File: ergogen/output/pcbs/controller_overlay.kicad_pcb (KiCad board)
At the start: 2 copper layers, 19.7 x 60.1 mm, 2 parts

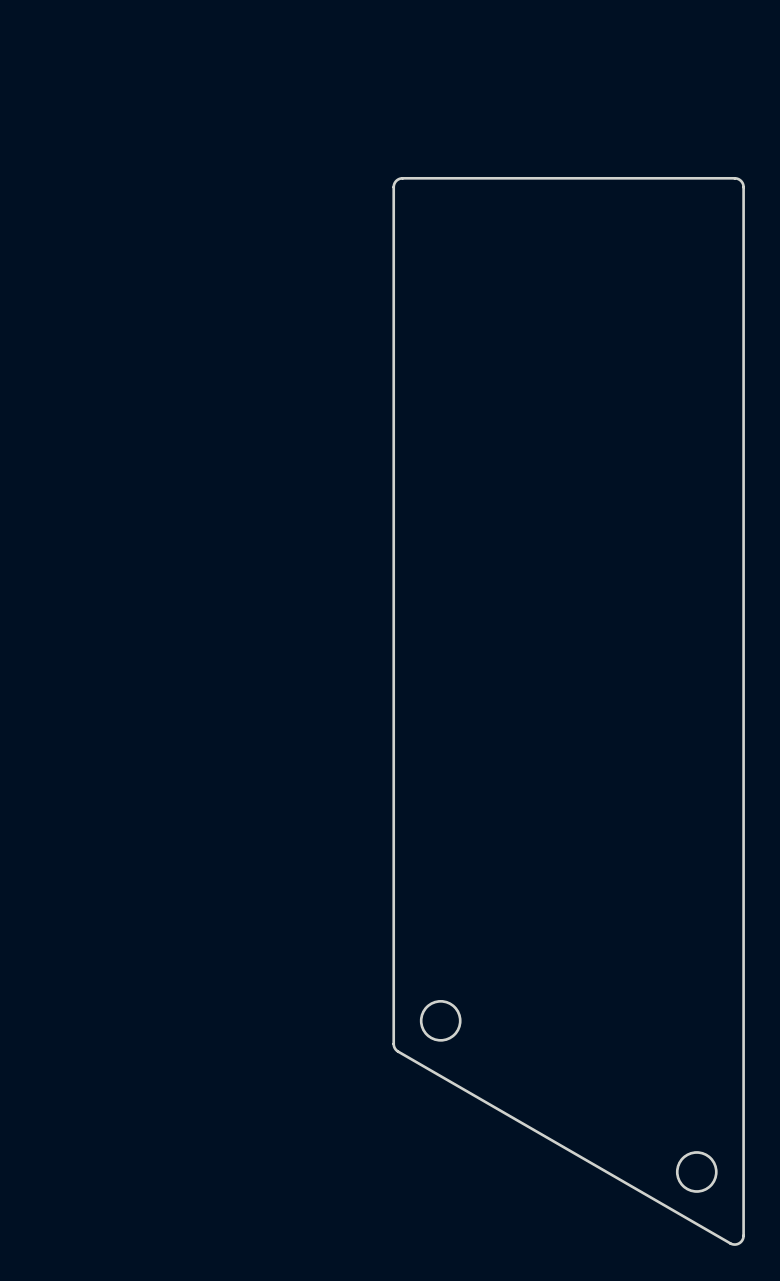
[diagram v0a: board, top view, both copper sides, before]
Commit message: Removed outer column
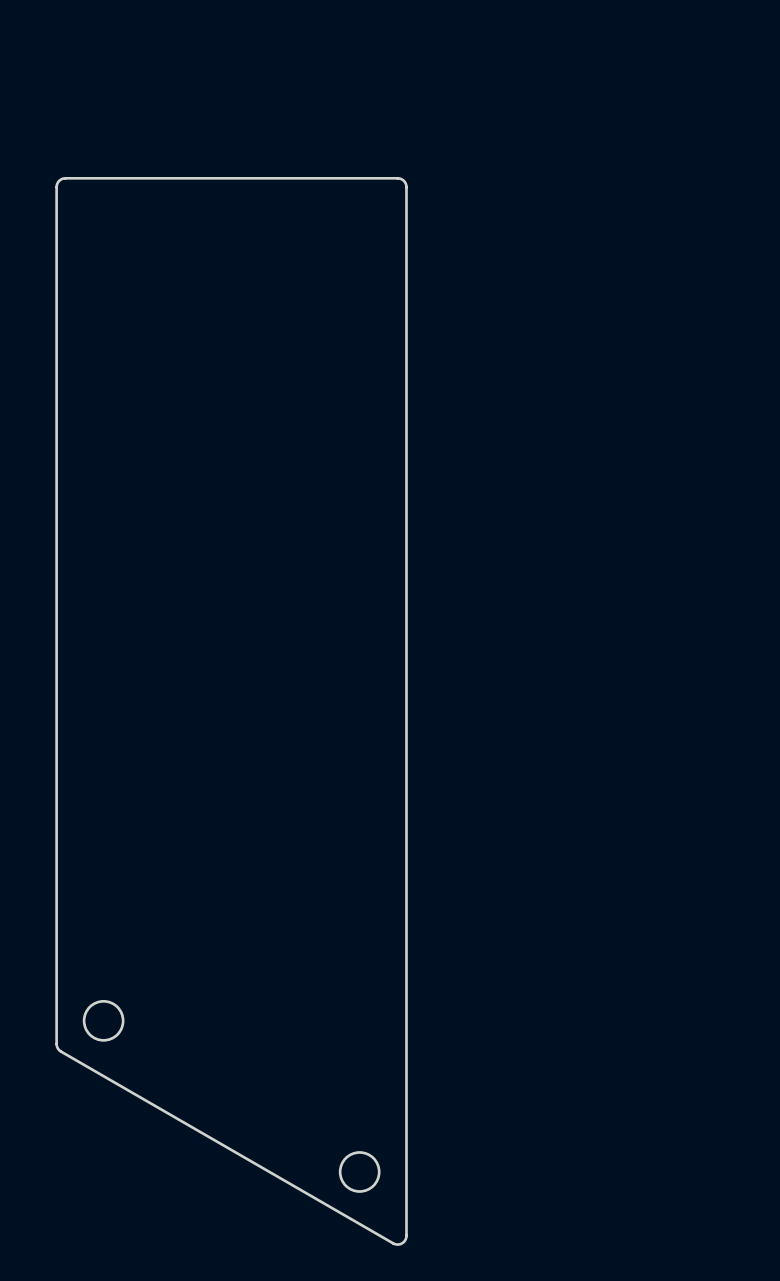
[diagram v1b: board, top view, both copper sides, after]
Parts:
- moved MH1 19.0 mm to (188.8, 100.5)
- moved MH2 19.0 mm to (203.2, 109.0)

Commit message: Changed stagger to be like karia
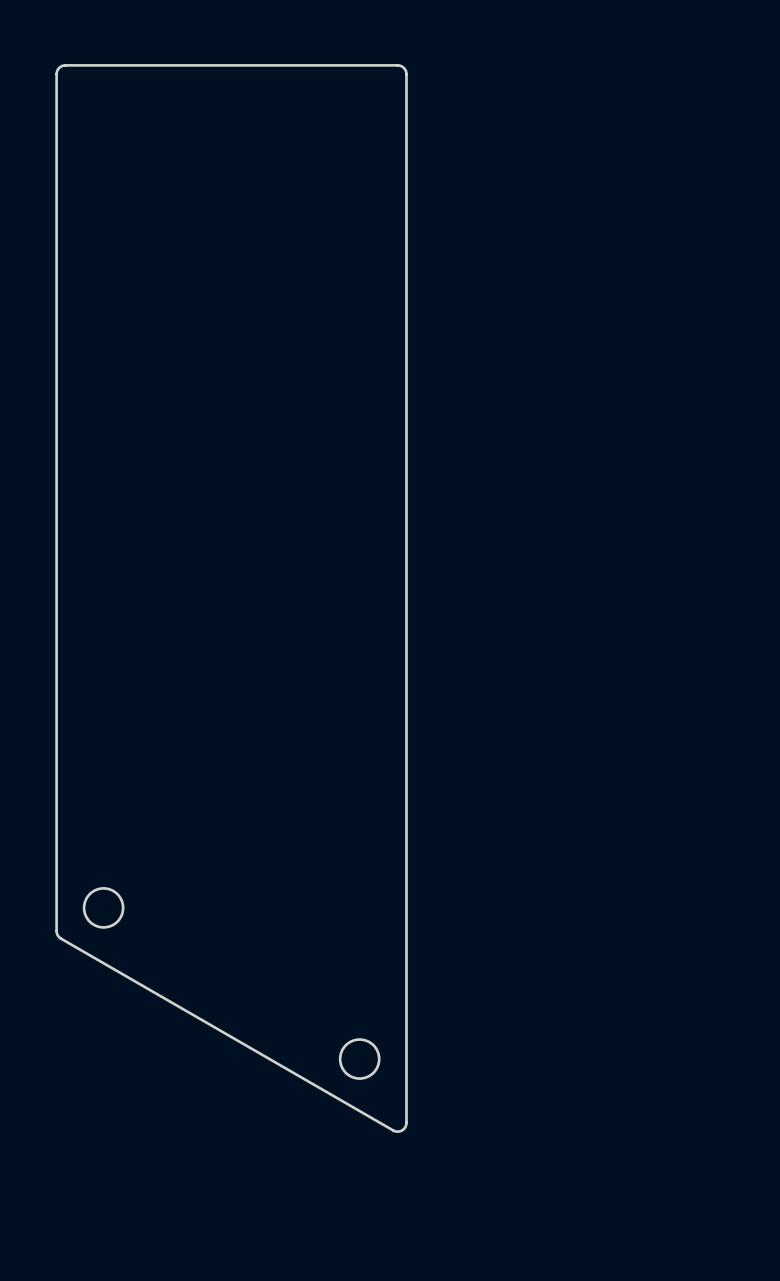
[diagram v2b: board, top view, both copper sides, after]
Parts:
- moved MH1 6.36 mm to (188.8, 94.1)
- moved MH2 6.36 mm to (203.2, 102.6)
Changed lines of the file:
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@@
   (net 0 "")
   (module "ceoloide:mounting_hole_npth" (layer F.Cu)
-      (at 188.762 100.476 0)
+      (at 188.762 94.111 0)
       (fp_text reference "MH1" (at 0 2.55 0) (layer F.SilkS) hide (effects (font (size 1 1) (thickness 0.15))))
       (pad "" np_thru_hole circle (at 0 0 0) (size 2.2 2.2) (drill 2.2) (layers *.Cu *.Mask))
   )
   (module "ceoloide:mounting_hole_npth" (layer F.Cu)
-      (at 203.194 108.995 0)
+      (at 203.194 102.63000000000001 0)
       (fp_text reference "MH2" (at 0 2.55 0) (layer F.SilkS) hide (effects (font (size 1 1) (thickness 0.15))))
       (pad "" np_thru_hole circle (at 0 0 0) (size 2.2 2.2) (drill 2.2) (layers *.Cu *.Mask))
   )
-  (gr_line (start 186.113 101.77697755907995) (end 186.113 53.49) (layer Edge.Cuts) (stroke (width 0.15) (type default)))
-(gr_line (start 186.613 52.99) (end 205.333 52.99) (layer Edge.Cuts) (stroke (width 0.15) (type default)))
-(gr_line (start 205.833 53.49) (end 205.833 112.58497459811555) (layer Edge.Cuts) (stroke (width 0.15) (type default)))
-(gr_line (start 205.083 113.01798729811556) (end 186.36299999999997 102.20999025907994) (layer Edge.Cuts) (stroke (width 0.15) (type default)))
-(gr_arc (start 186.613 52.99) (mid 186.2594466 53.1364466) (end 186.113 53.49) (layer Edge.Cuts) (stroke (width 0.15) (type default)))
-(gr_arc (start 205.833 53.49) (mid 205.6865534 53.1364466) (end 205.333 52.99) (layer Edge.Cuts) (stroke (width 0.15) (type default)))
-(gr_arc (start 205.083 113.01798729811556) (mid 205.583 113.01798729811556) (end 205.833 112.58497459811555) (layer Edge.Cuts) (stroke (width 0.15) (type default)))
-(gr_arc (start 186.113 101.77697755907995) (mid 186.1799873 102.02697755907995) (end 186.363 102.20999025907996) (layer Edge.Cuts) (stroke (width 0.15) (type default)))
-(gr_circle (center 188.762 100.476) (end 189.862 100.476) (layer Edge.Cuts) (stroke (width 0.15) (type default)) (fill none))
-(gr_circle (center 203.194 108.995) (end 204.29399999999998 108.995) (layer Edge.Cuts) (stroke (width 0.15) (type default)) (fill none))
+  (gr_line (start 186.113 95.41197755907994) (end 186.113 47.12500000000001) (layer Edge.Cuts) (stroke (width 0.15) (type default)))
+(gr_line (start 186.613 46.62500000000001) (end 205.333 46.62500000000001) (layer Edge.Cuts) (stroke (width 0.15) (type default)))
+(gr_line (start 205.833 47.12500000000001) (end 205.833 106.21997459811557) (layer Edge.Cuts) (stroke (width 0.15) (type default)))
+(gr_line (start 205.08300000000003 106.65298729811559) (end 186.363 95.84499025907995) (layer Edge.Cuts) (stroke (width 0.15) (type default)))
+(gr_arc (start 186.613 46.62500000000001) (mid 186.2594466 46.771446600000004) (end 186.113 47.12500000000001) (layer Edge.Cuts) (stroke (width 0.15) (type default)))
+(gr_arc (start 205.833 47.12500000000001) (mid 205.6865534 46.771446600000004) (end 205.333 46.62500000000001) (layer Edge.Cuts) (stroke (width 0.15) (type default)))
+(gr_arc (start 205.083 106.65298729811558) (mid 205.583 106.65298729811558) (end 205.833 106.21997459811557) (layer Edge.Cuts) (stroke (width 0.15) (type default)))
+(gr_arc (start 186.113 95.41197755907994) (mid 186.1799873 95.66197755907994) (end 186.363 95.84499025907995) (layer Edge.Cuts) (stroke (width 0.15) (type default)))
+(gr_circle (center 188.762 94.111) (end 189.862 94.111) (layer Edge.Cuts) (stroke (width 0.15) (type default)) (fill none))
+(gr_circle (center 203.194 102.63000000000001) (end 204.29399999999998 102.63000000000001) (layer Edge.Cuts) (stroke (width 0.15) (type default)) (fill none))
 )

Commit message: Added splay to pinky
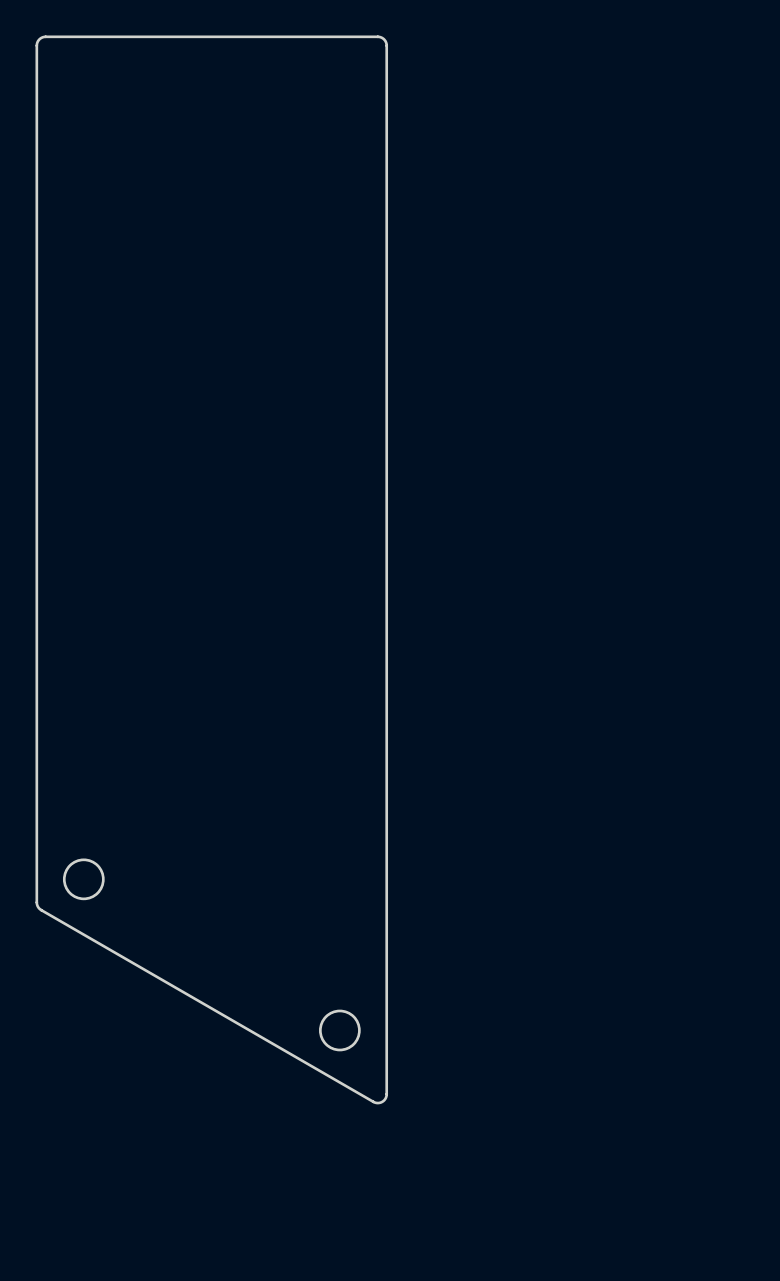
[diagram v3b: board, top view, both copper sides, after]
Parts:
- moved MH1 1.96 mm to (187.6, 92.5)
- moved MH2 1.96 mm to (202.1, 101.0)
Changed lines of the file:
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@@
   (net 0 "")
   (module "ceoloide:mounting_hole_npth" (layer F.Cu)
-      (at 188.762 94.111 0)
+      (at 187.6464451 92.50059040000001 0)
       (fp_text reference "MH1" (at 0 2.55 0) (layer F.SilkS) hide (effects (font (size 1 1) (thickness 0.15))))
       (pad "" np_thru_hole circle (at 0 0 0) (size 2.2 2.2) (drill 2.2) (layers *.Cu *.Mask))
   )
   (module "ceoloide:mounting_hole_npth" (layer F.Cu)
-      (at 203.194 102.63000000000001 0)
+      (at 202.07844509999998 101.01959040000001 0)
       (fp_text reference "MH2" (at 0 2.55 0) (layer F.SilkS) hide (effects (font (size 1 1) (thickness 0.15))))
       (pad "" np_thru_hole circle (at 0 0 0) (size 2.2 2.2) (drill 2.2) (layers *.Cu *.Mask))
   )
-  (gr_line (start 186.113 95.41197755907994) (end 186.113 47.12500000000001) (layer Edge.Cuts) (stroke (width 0.15) (type default)))
-(gr_line (start 186.613 46.62500000000001) (end 205.333 46.62500000000001) (layer Edge.Cuts) (stroke (width 0.15) (type default)))
-(gr_line (start 205.833 47.12500000000001) (end 205.833 106.21997459811557) (layer Edge.Cuts) (stroke (width 0.15) (type default)))
-(gr_line (start 205.08300000000003 106.65298729811559) (end 186.363 95.84499025907995) (layer Edge.Cuts) (stroke (width 0.15) (type default)))
-(gr_arc (start 186.613 46.62500000000001) (mid 186.2594466 46.771446600000004) (end 186.113 47.12500000000001) (layer Edge.Cuts) (stroke (width 0.15) (type default)))
-(gr_arc (start 205.833 47.12500000000001) (mid 205.6865534 46.771446600000004) (end 205.333 46.62500000000001) (layer Edge.Cuts) (stroke (width 0.15) (type default)))
-(gr_arc (start 205.083 106.65298729811558) (mid 205.583 106.65298729811558) (end 205.833 106.21997459811557) (layer Edge.Cuts) (stroke (width 0.15) (type default)))
-(gr_arc (start 186.113 95.41197755907994) (mid 186.1799873 95.66197755907994) (end 186.363 95.84499025907995) (layer Edge.Cuts) (stroke (width 0.15) (type default)))
-(gr_circle (center 188.762 94.111) (end 189.862 94.111) (layer Edge.Cuts) (stroke (width 0.15) (type default)) (fill none))
-(gr_circle (center 203.194 102.63000000000001) (end 204.29399999999998 102.63000000000001) (layer Edge.Cuts) (stroke (width 0.15) (type default)) (fill none))
+  (gr_line (start 184.9974451 93.8015679590799) (end 184.9974451 45.51459040000001) (layer Edge.Cuts) (stroke (width 0.15) (type default)))
+(gr_line (start 185.4974451 45.01459040000001) (end 204.2174451 45.01459040000001) (layer Edge.Cuts) (stroke (width 0.15) (type default)))
+(gr_line (start 204.7174451 45.51459040000001) (end 204.7174451 104.60956499811556) (layer Edge.Cuts) (stroke (width 0.15) (type default)))
+(gr_line (start 203.9674451 105.04257769811556) (end 185.2474451 94.23458065907991) (layer Edge.Cuts) (stroke (width 0.15) (type default)))
+(gr_arc (start 185.4974451 45.01459040000001) (mid 185.14389169999998 45.16103700000001) (end 184.9974451 45.51459040000001) (layer Edge.Cuts) (stroke (width 0.15) (type default)))
+(gr_arc (start 204.7174451 45.51459040000001) (mid 204.5709985 45.16103700000001) (end 204.2174451 45.01459040000001) (layer Edge.Cuts) (stroke (width 0.15) (type default)))
+(gr_arc (start 203.9674451 105.04257769811556) (mid 204.4674451 105.04257769811556) (end 204.7174451 104.60956499811556) (layer Edge.Cuts) (stroke (width 0.15) (type default)))
+(gr_arc (start 184.9974451 93.8015679590799) (mid 185.0644324 94.0515679590799) (end 185.2474451 94.23458065907991) (layer Edge.Cuts) (stroke (width 0.15) (type default)))
+(gr_circle (center 187.6464451 92.50059040000001) (end 188.7464451 92.50059040000001) (layer Edge.Cuts) (stroke (width 0.15) (type default)) (fill none))
+(gr_circle (center 202.07844509999998 101.01959040000001) (end 203.17844509999998 101.01959040000001) (layer Edge.Cuts) (stroke (width 0.15) (type default)) (fill none))
 )

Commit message: Tweak shape
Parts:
- removed MH1, MH2: , ceoloide:mounting_hole_npth
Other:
- board size 19.7 x 60.1 mm -> 19.7 x 54.6 mm
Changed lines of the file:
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@@
   )
   (net 0 "")
-  (module "ceoloide:mounting_hole_npth" (layer F.Cu)
-      (at 187.6464451 92.50059040000001 0)
-      (fp_text reference "MH1" (at 0 2.55 0) (layer F.SilkS) hide (effects (font (size 1 1) (thickness 0.15))))
-      (pad "" np_thru_hole circle (at 0 0 0) (size 2.2 2.2) (drill 2.2) (layers *.Cu *.Mask))
-  )
-  (module "ceoloide:mounting_hole_npth" (layer F.Cu)
-      (at 202.07844509999998 101.01959040000001 0)
-      (fp_text reference "MH2" (at 0 2.55 0) (layer F.SilkS) hide (effects (font (size 1 1) (thickness 0.15))))
-      (pad "" np_thru_hole circle (at 0 0 0) (size 2.2 2.2) (drill 2.2) (layers *.Cu *.Mask))
-  )
-  (gr_line (start 184.9974451 93.8015679590799) (end 184.9974451 45.51459040000001) (layer Edge.Cuts) (stroke (width 0.15) (type default)))
+  (gr_line (start 184.9974451 88.34056795907989) (end 184.9974451 45.51459040000001) (layer Edge.Cuts) (stroke (width 0.15) (type default)))
 (gr_line (start 185.4974451 45.01459040000001) (end 204.2174451 45.01459040000001) (layer Edge.Cuts) (stroke (width 0.15) (type default)))
-(gr_line (start 204.7174451 45.51459040000001) (end 204.7174451 104.60956499811556) (layer Edge.Cuts) (stroke (width 0.15) (type default)))
-(gr_line (start 203.9674451 105.04257769811556) (end 185.2474451 94.23458065907991) (layer Edge.Cuts) (stroke (width 0.15) (type default)))
+(gr_line (start 204.7174451 45.51459040000001) (end 204.7174451 99.14856499811555) (layer Edge.Cuts) (stroke (width 0.15) (type default)))
+(gr_line (start 203.9674451 99.58157769811555) (end 185.2474451 88.7735806590799) (layer Edge.Cuts) (stroke (width 0.15) (type default)))
 (gr_arc (start 185.4974451 45.01459040000001) (mid 185.14389169999998 45.16103700000001) (end 184.9974451 45.51459040000001) (layer Edge.Cuts) (stroke (width 0.15) (type default)))
 (gr_arc (start 204.7174451 45.51459040000001) (mid 204.5709985 45.16103700000001) (end 204.2174451 45.01459040000001) (layer Edge.Cuts) (stroke (width 0.15) (type default)))
-(gr_arc (start 203.9674451 105.04257769811556) (mid 204.4674451 105.04257769811556) (end 204.7174451 104.60956499811556) (layer Edge.Cuts) (stroke (width 0.15) (type default)))
-(gr_arc (start 184.9974451 93.8015679590799) (mid 185.0644324 94.0515679590799) (end 185.2474451 94.23458065907991) (layer Edge.Cuts) (stroke (width 0.15) (type default)))
-(gr_circle (center 187.6464451 92.50059040000001) (end 188.7464451 92.50059040000001) (layer Edge.Cuts) (stroke (width 0.15) (type default)) (fill none))
-(gr_circle (center 202.07844509999998 101.01959040000001) (end 203.17844509999998 101.01959040000001) (layer Edge.Cuts) (stroke (width 0.15) (type default)) (fill none))
+(gr_arc (start 203.9674451 99.58157769811555) (mid 204.4674451 99.58157769811555) (end 204.7174451 99.14856499811555) (layer Edge.Cuts) (stroke (width 0.15) (type default)))
+(gr_arc (start 184.9974451 88.34056795907989) (mid 185.0644324 88.59056795907989) (end 185.2474451 88.7735806590799) (layer Edge.Cuts) (stroke (width 0.15) (type default)))
 )
